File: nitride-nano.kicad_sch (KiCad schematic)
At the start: 1 part, among them J3 Conn_01x04_Pin

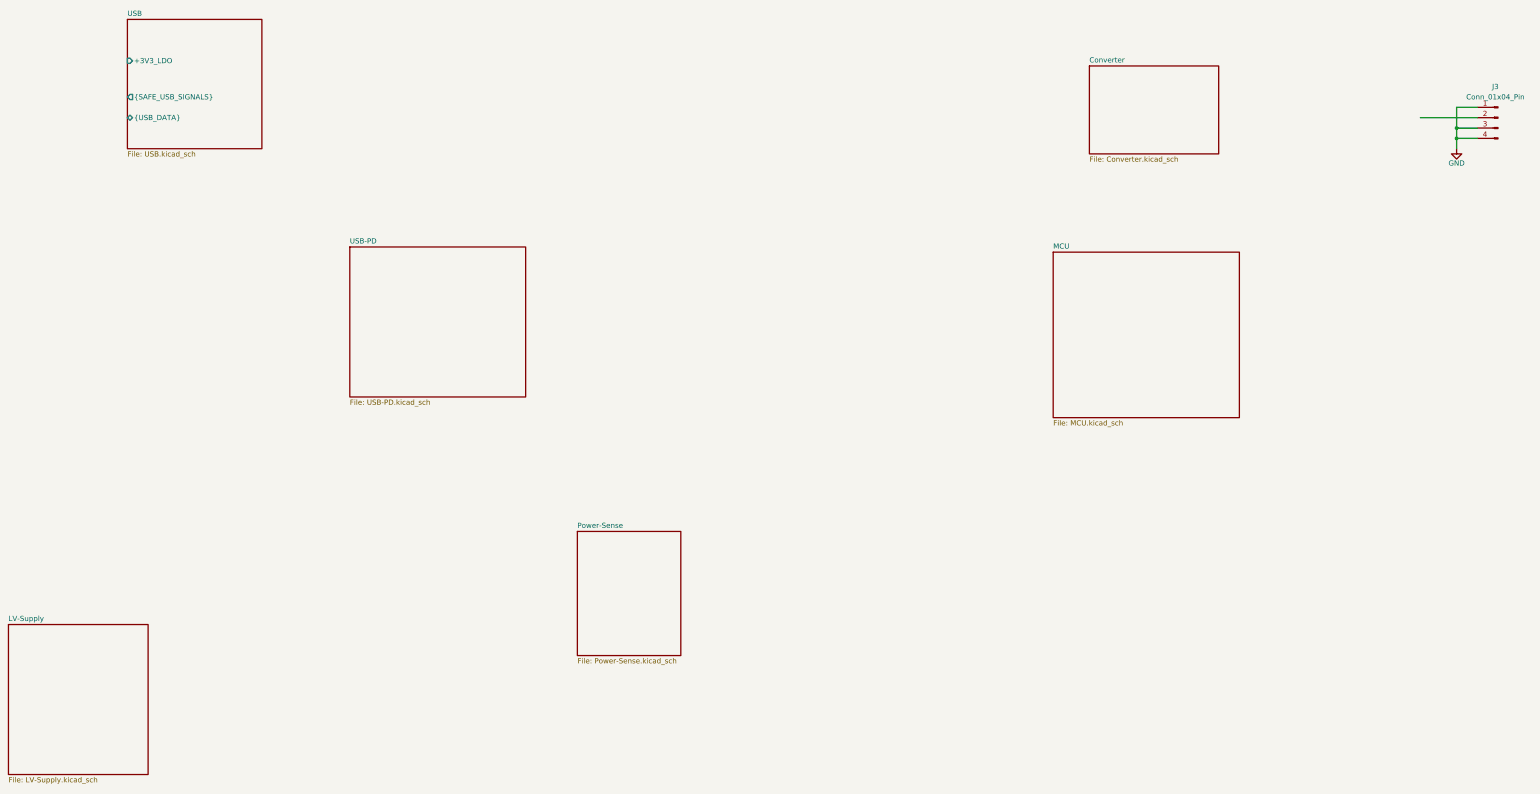
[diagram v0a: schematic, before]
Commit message: Cleaned up the hierarchy
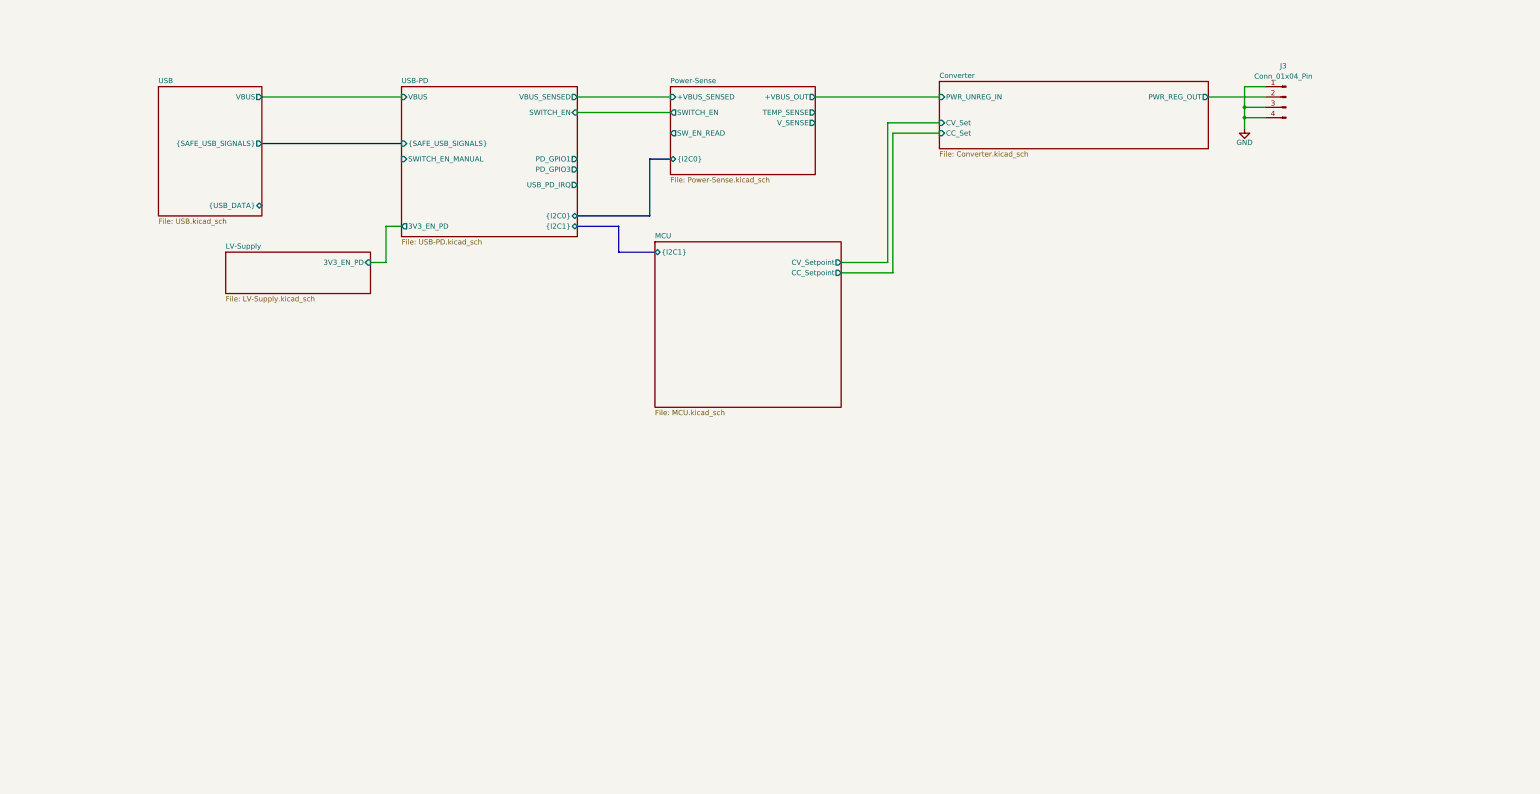
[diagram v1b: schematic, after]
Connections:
- net Converter/PWR_REG_OUT: now reaches J3.2 (Pin_2)
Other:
- sheet Converter ports: added CC_Set, CV_Set, PWR_REG_OUT, PWR_UNREG_IN; removed none
- sheet LV-Supply ports: added 3V3_EN_PD; removed none
- sheet MCU ports: added CC_Setpoint, CV_Setpoint, {I2C1}; removed none
- sheet Power-Sense ports: added +VBUS_OUT, +VBUS_SENSED, SWITCH_EN, SW_EN_READ, TEMP_SENSE, V_SENSE, {I2C0}; removed none
- sheet USB ports: added VBUS; removed +3V3_LDO
- sheet USB-PD ports: added 3V3_EN_PD, PD_GPIO1, PD_GPIO3, SWITCH_EN, SWITCH_EN_MANUAL, USB_PD_IRQ, VBUS, VBUS_SENSED, {I2C0}, {I2C1}, {SAFE_USB_SIGNALS}; removed none
- moved on the sheet: J3

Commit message: inductor, output fets
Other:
- sheet Converter ports: added Curr_FB; removed none
- sheet MCU ports: added Current_Feedback; removed none
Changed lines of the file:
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@@
+	(wire
+		(pts
+			(xy 242.57 149.86) (xy 242.57 115.57)
+		)
+		(stroke
+			(width 0)
+			(type default)
+		)
+	)
 	(wire
 		(pts
@@
 	(wire
 		(pts
+			(xy 242.57 115.57) (xy 252.73 115.57)
+		)
+		(stroke
+			(width 0)
+			(type default)
+		)
+	)
+	(wire
+		(pts
 			(xy 86.36 104.14) (xy 120.65 104.14)
 		)
@@
 		(pts
 			(xy 163.83 133.35) (xy 181.61 133.35)
+		)
+		(stroke
+			(width 0)
+			(type default)
+		)
+	)
+	(wire
+		(pts
+			(xy 228.6 149.86) (xy 242.57 149.86)
 		)
 		(stroke
@@
 			)
 		)
+		(pin "Current_Feedback" input
+			(at 228.6 149.86 0)
+			(effects
+				(font
+					(size 1.27 1.27)
+				)
+				(justify right)
+			)
+		)
 		(instances
 			(project "nitride-nano"
@@
 			)
 		)
+		(pin "Curr_FB" output
+			(at 252.73 115.57 180)
+			(effects
+				(font
+					(size 1.27 1.27)
+				)
+				(justify left)
+			)
+		)

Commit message: Starting with layout, oled, encoder, xt90
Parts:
- added F1: 10A, Fuse:Fuse_1210_3225Metric, symbol Device:Fuse
- added H1, H2, H3, H4: MountingHole_Pad, MountingHole:MountingHole_3.2mm_M3_Pad_Via, symbol Mechanical:MountingHole_Pad
- added J6: Conn_01x04_Pin, thommys-parts2:CONN-TH_XT90PW-M, symbol Connector:Conn_01x04_Pin
- J3: JLC (none) -> C3040689
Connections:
- net GND: now also H1.1, H2.1, H3.1, H4.1, J6.2 (Pin_2), J6.3 (Pin_3), J6.4 (Pin_4)
- net Power-Sense/+VBUS_SENSED: now also F1.2
- new net: F1.1, J6.1 (Pin_1)
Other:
- sheet MCU ports: added Bus voltage, Temp, {USB_DATA}; removed none

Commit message: Finished layout
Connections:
- net VPP: now reaches F1.1, J6.1 (Pin_1)
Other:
- sheet Converter ports: added TEMP_SENSE_CONV; removed none
- sheet MCU ports: added PD_GPIO1, PD_GPIO3, SWITCH_EN_MANUAL, SWITCH_EN_READ, Temp Converter, Temp PWR In, USB_PD_IRQ; removed Temp
- sheet Power-Sense ports: added TEMP_SENSE_PWRIN; removed TEMP_SENSE
- moved on the sheet: H1, H2, H3, H4, J3

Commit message: Started routing
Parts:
- added D16, D17: SMAJ58A, PCM_JLCPCB:D_SMA, symbol PCM_JLCPCB-Diodes:TVS-Uni,SMAJ58A
- added D18, D21: LED, LED_SMD:LED_0603_1608Metric, symbol Device:LED
- added R30, R76: 10k, Resistor_SMD:R_0402_1005Metric, symbol Device:R
- F1: footprint Fuse:Fuse_1210_3225Metric -> Fuse:Fuse_1812_4532Metric
- J3: value Conn_01x04_Pin -> XT-90-M
- J6: value Conn_01x04_Pin -> XT90-F
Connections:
- net Converter/PWR_REG_OUT: now also D17.1, D21.2 (A)
- net GND: now also D16.2, D17.2, R30.1, R76.1
- net VPP: now also D16.1, D18.2 (A)
- new net: D18.1 (K), R30.2
- new net: D21.1 (K), R76.2
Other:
- sheet Converter ports: added Conv-Disable, Vsense_REG_OUT; removed none
- sheet MCU ports: added Converter-Disable, Vsense_REG_OUT; removed none
- note added: "TODO: Fix LV supply transient"
- note added: "TODO: Output V sensing"
- company: (none) -> Picobello B.V.
- title: (none) -> Nitride-Nano
- moved on the sheet: F1, J3, J6

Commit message: 20A fuse
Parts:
- F1: value 10A -> 20A
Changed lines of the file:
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@@
 			)
 		)
-		(property "Value" "10A"
+		(property "Value" "20A"
 			(at 180.34 83.8199 0)
 			(show_name no)

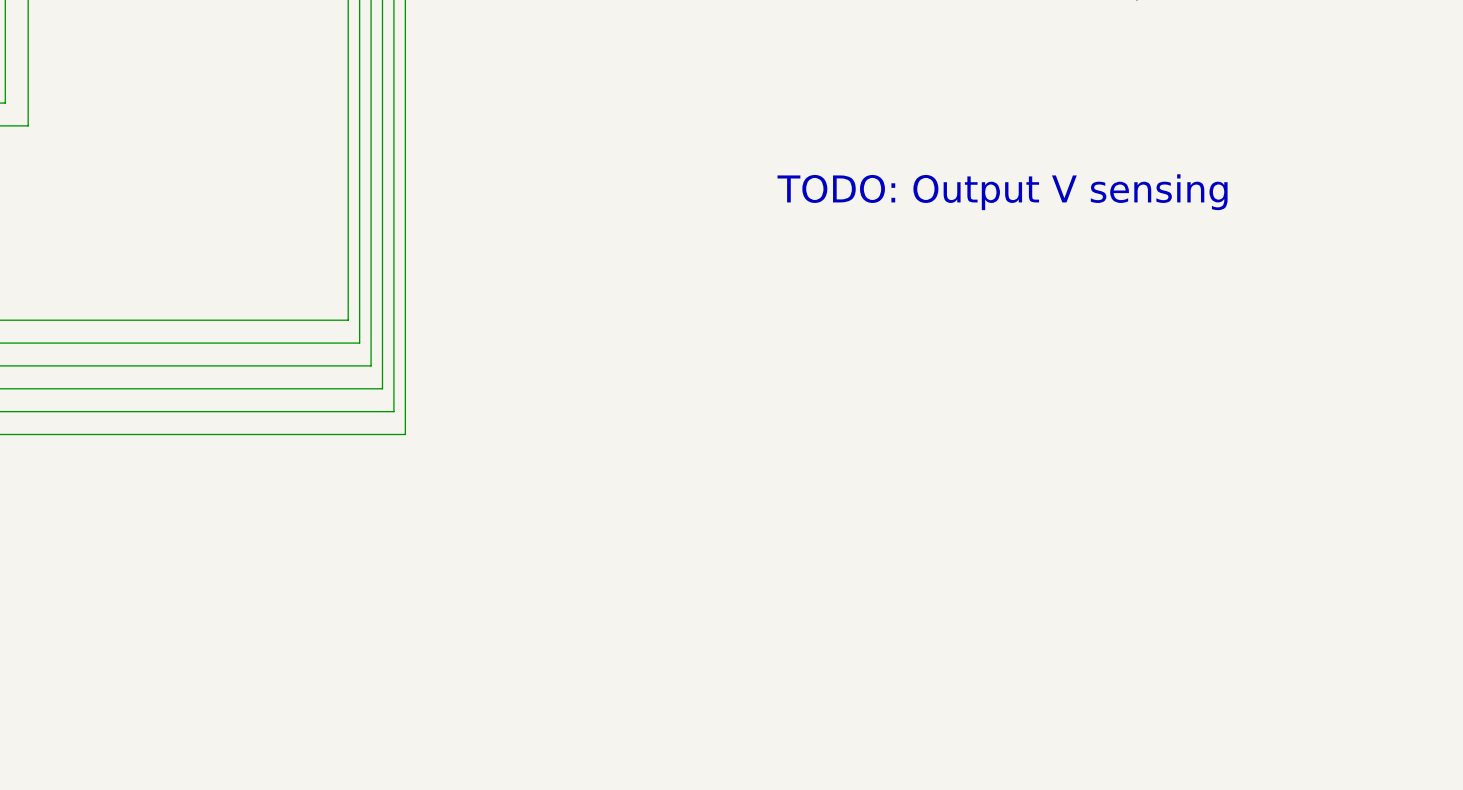
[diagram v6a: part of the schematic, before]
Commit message: fixed pinout of cpu, added freecad file for the housing
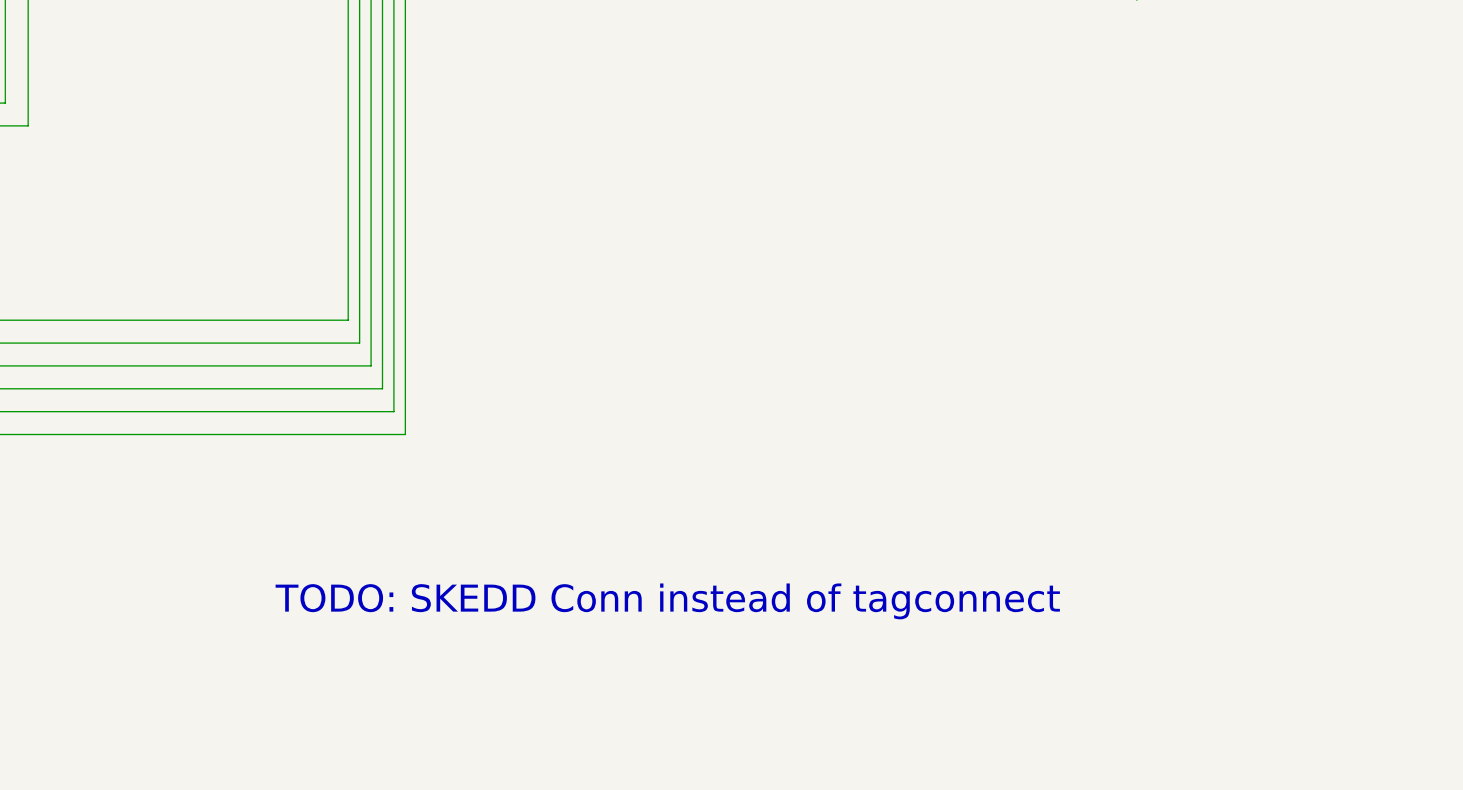
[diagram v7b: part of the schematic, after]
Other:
- note added: "TODO: SKEDD Conn instead of tagconnect"
- note removed: "TODO: Output V sensing"
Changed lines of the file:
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@@
 		)
 	)
-	(text "TODO: Output V sensing"
+	(text "TODO: SKEDD Conn instead of tagconnect"
 		(exclude_from_sim no)
-		(at 343.408 152.146 0)
+		(at 306.07 197.612 0)
 		(effects
 			(font
